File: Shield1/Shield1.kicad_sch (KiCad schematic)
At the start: 26 parts, among them J1 Conn_01x01_Male, J10 Conn_01x01_Male, J11 Conn_01x01_Male, J12 Conn_01x01_Male, J13 Conn_01x01_Male, J14 Conn_01x01_Male, J15 Conn_01x01_Male, J16 Conn_01x01_Male, J17 Conn_01x01_Male, J18 Conn_01x01_Male, J19 Conn_01x01_Male, J2 Conn_01x01_Male, J3 Conn_01x01_Male, J4 Conn_01x01_Male, J5 Conn_01x01_Male, J6 Conn_01x01_Male, J7 Conn_01x01_Male, J8 Conn_01x01_Male, J9 Conn_01x01_Male, X1 USB_C_24pins

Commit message: v0.6 actual state
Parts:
- gave numbers to parts that had none: 2
- renumbered J8 to J10, J9 to J11, J10 to J12, J11 to J13, J12 to J14, J13 to J15, J14 to J16, J15 to J17, J16 to J18, J17 to J19, J18 to J20, J19 to J21, J1 to J3, J2 to J4, J3 to J5, J4 to J6, J5 to J7, J6 to J8, J7 to J9

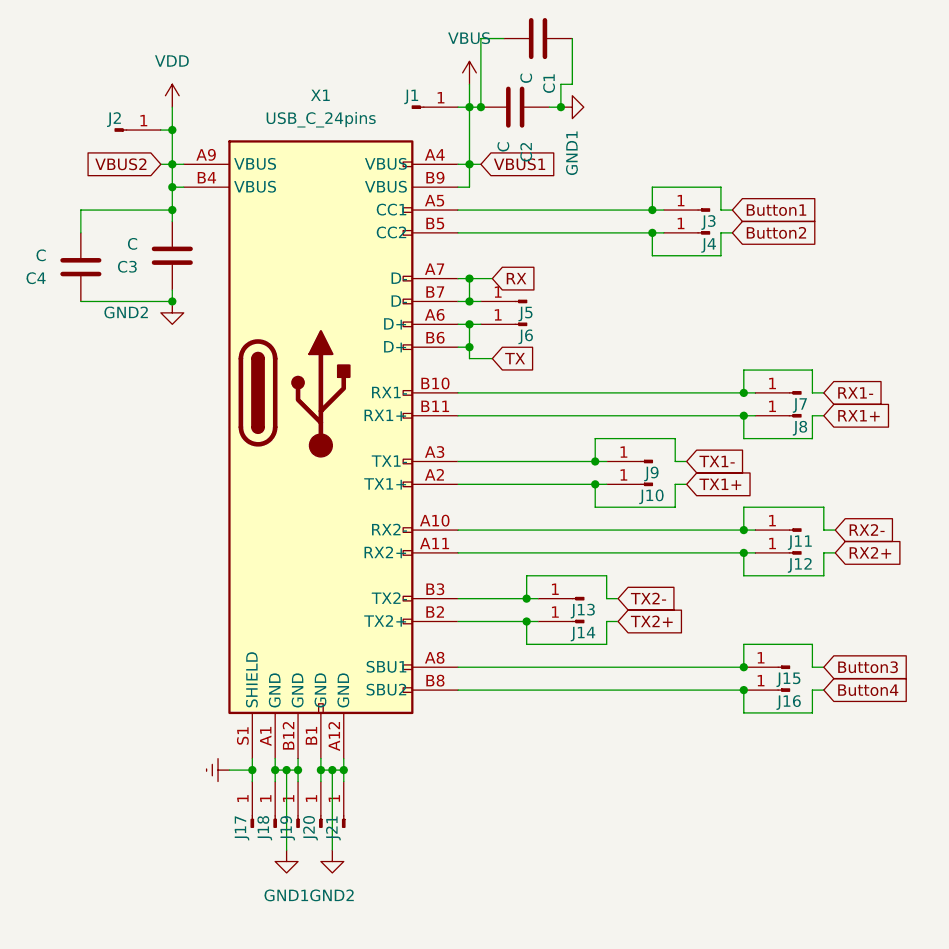
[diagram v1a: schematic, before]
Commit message: v0.7 Circuit has been corrected
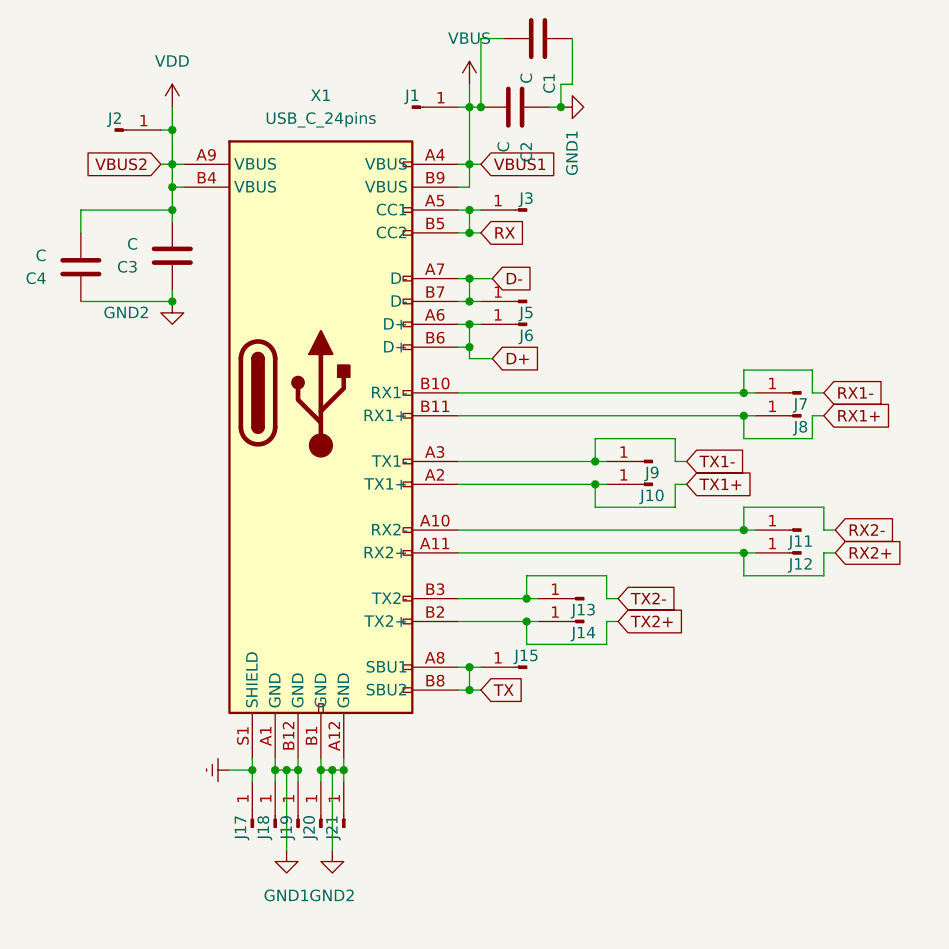
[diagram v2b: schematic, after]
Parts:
- removed J16, J4: Conn_01x01_Male, Shield1:throughPin, symbol Connector:Conn_01x01_Male
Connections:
- net Button1 is gone; now on net RX: J3.1 (Pin_1), X1.A5 (CC1)
- net Button2 is gone; now on net RX: X1.B5 (CC2)
- net Button3 is gone; now on net TX: J15.1 (Pin_1), X1.A8 (SBU1)
- net Button4 is gone; now on net TX: X1.B8 (SBU2)
- net RX: no longer J5.1 (Pin_1), X1.A7 (D-), X1.B7 (D-)
- net TX: no longer J6.1 (Pin_1), X1.A6 (D+), X1.B6 (D+)
- new net D+: J6.1 (Pin_1), X1.A6 (D+), X1.B6 (D+)
- new net D-: J5.1 (Pin_1), X1.A7 (D-), X1.B7 (D-)
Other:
- moved on the sheet: J15, J3

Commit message: v0.92 all the nets have been routed
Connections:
- net Earth: now also X1.S2 (SHIELD), X1.S3 (SHIELD), X1.S4 (SHIELD)
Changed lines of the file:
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@@
     (pin "B8")
     (pin "B9")
+    (pin "S3")
+    (pin "S4")
     (pin "S1")
+    (pin "S2")
   )
   (symbol (lib_id "Device:C") (at 104.14 54.61 180) (unit 1)

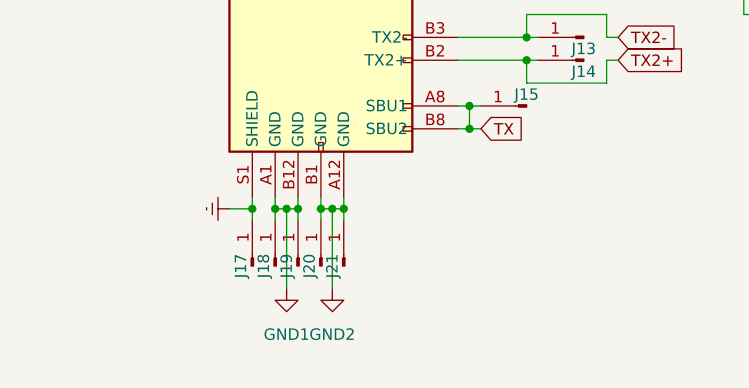
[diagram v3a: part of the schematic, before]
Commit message: v0.94 cir-pcb connection has been restored
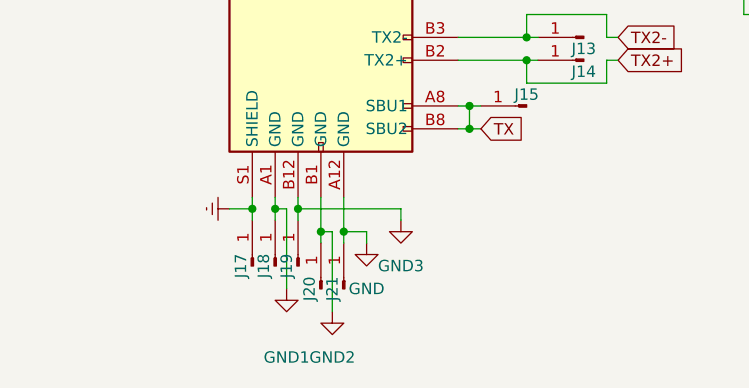
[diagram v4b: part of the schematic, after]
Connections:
- net GND1: no longer J19.1 (Pin_1), X1.B12 (GND)
- net GND2: no longer J21.1 (Pin_1), X1.A12 (GND)
- new net GND: J21.1 (Pin_1), X1.A12 (GND)
- new net GND3: J19.1 (Pin_1), X1.B12 (GND)
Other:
- moved on the sheet: J20, J21

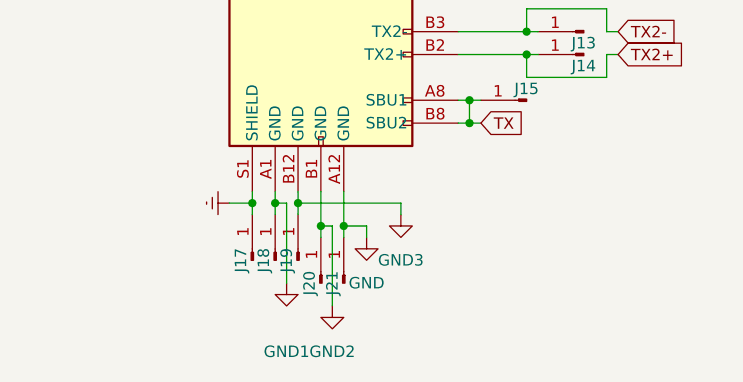
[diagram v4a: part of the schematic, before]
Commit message: v0.99 GND has been corrected
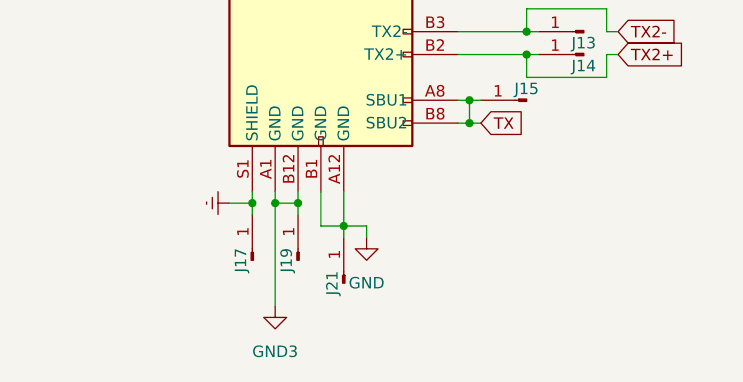
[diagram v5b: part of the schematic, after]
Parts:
- removed J18, J20: Conn_01x01_Male, Shield1:smdPin, symbol Connector:Conn_01x01_Male
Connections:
- net GND: now also X1.B1 (GND)
- net GND1: no longer X1.A1 (GND)
- net GND2: no longer X1.B1 (GND)
- net GND3: now also X1.A1 (GND)
